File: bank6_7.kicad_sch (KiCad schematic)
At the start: 1 part, among them IC1 ECP5-BGA256

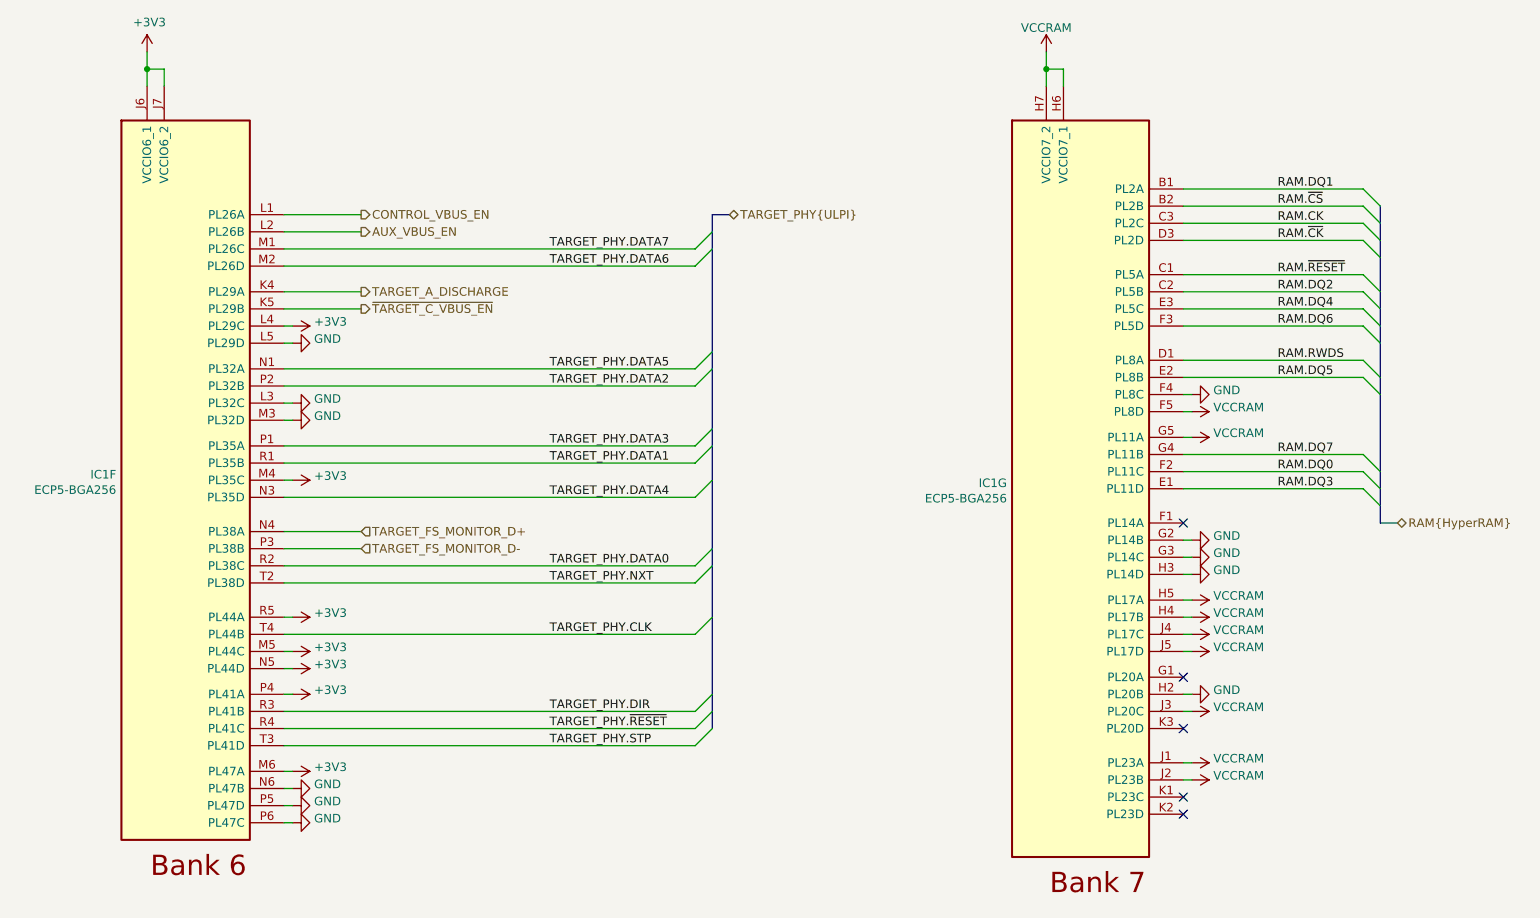
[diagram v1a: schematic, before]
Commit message: Clean up schematic
- Renumber Pmod signal names to match silkscreen labels
- Clean up FPGA symbol
- Clean up PHY symbol
- Add title block to newer sheets
- Fix horizontal line in LED sheet
- Improve various label positions
- Update data sheet fields
- Renumber pages
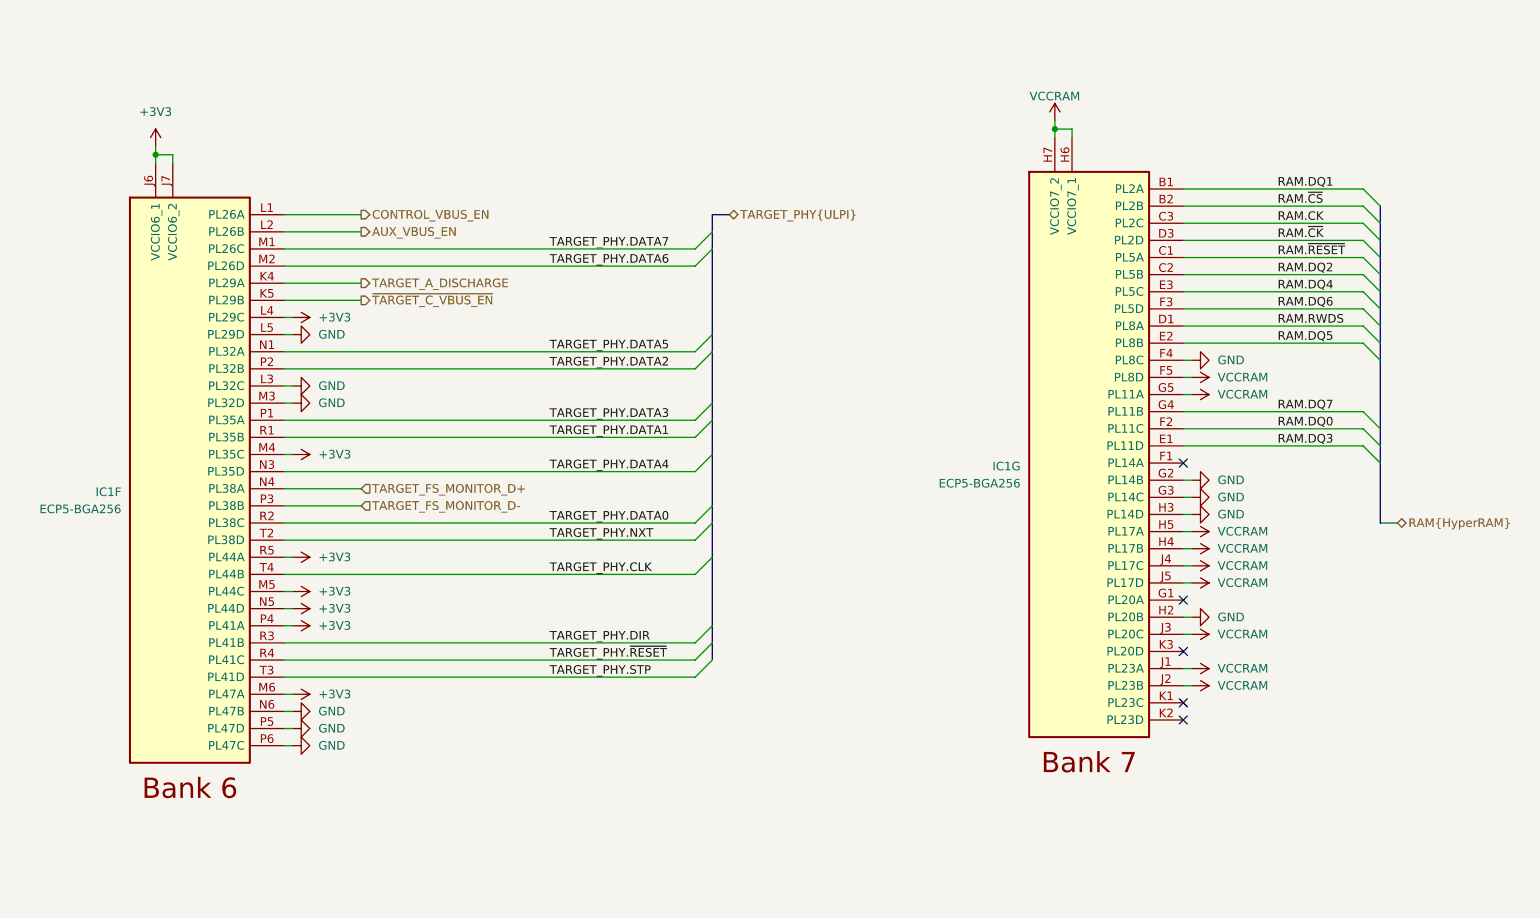
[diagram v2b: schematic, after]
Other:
- moved on the sheet: IC1F, IC1G

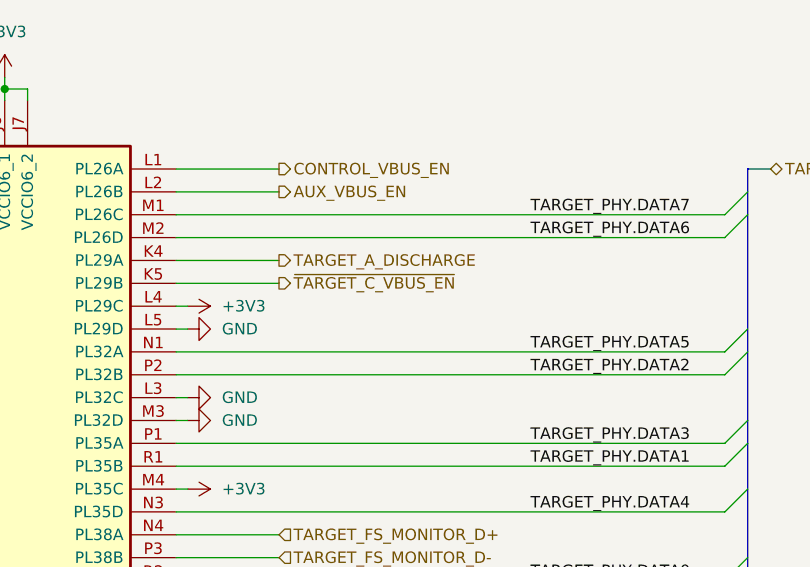
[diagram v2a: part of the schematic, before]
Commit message: Change TARGET_C_VBUS pass-through default
Previously pass-through power between TARGET C and TARGET A was enabled
by default, even when the Cynthion was unpowered. This had the potential
benefit of allowing a pass-through target device to function while the
Cynthion was off, but the feature was unreliable due to loading of D+/D-
by the PHY and TARGET_FS_MONITOR connections. All pass-through power is
now disabled by default, providing a consistent user experience while
the Cynthion is unpowered.
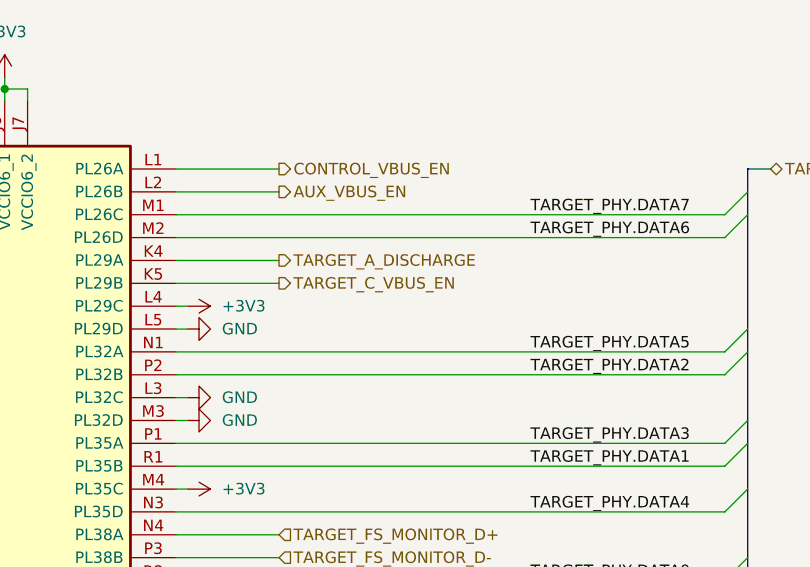
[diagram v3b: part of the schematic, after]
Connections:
- net ~{TARGET_C_VBUS_EN} renamed TARGET_C_VBUS_EN
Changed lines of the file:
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@@
     (effects (font (size 1.27 1.27)) (justify left))
   )
-  (hierarchical_label "~{TARGET_C_VBUS_EN}" (shape output) (at 68.58 68.58 0) (fields_autoplaced)
+  (hierarchical_label "TARGET_C_VBUS_EN" (shape output) (at 68.58 68.58 0) (fields_autoplaced)
     (effects (font (size 1.27 1.27)) (justify left))
   )

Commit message: Update copyright notices
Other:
- company: Copyright 2019-2023 Great Scott Gadgets -> ${COPYRIGHT}
- title: Cynthion -> ${TITLE}
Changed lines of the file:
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@@
   (paper "A4")
   (title_block
-    (title "Cynthion")
+    (title "${TITLE}")
     (date "${DATE}")
     (rev "${VERSION}")
-    (company "Copyright 2019-2023 Great Scott Gadgets")
-    (comment 1 "Licensed under the CERN-OHL-P v2")
+    (company "${COPYRIGHT}")
+    (comment 1 "${LICENSE}")
   )
   (junction (at 38.1 46.99) (diameter 0) (color 0 0 0 0)
